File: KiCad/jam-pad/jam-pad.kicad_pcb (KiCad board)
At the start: 2 copper layers, 173 x 57.1 mm, 56 parts, among them J1 USB_C, J2 PH_01x03_2.54mm, SW1 MX_Hotswap, SW13 SW_Push, SW14 RotaryEncoder_Switch, SW15 SW_Push, SW2 MX_Hotswap, SW3 MX_Hotswap, SW4 MX_Hotswap, SW5 MX_Hotswap, SW6 MX_Hotswap, SW7 MX_Hotswap, SW8 MX_Hotswap, SW9 MX_Hotswap, U1 RP2040, U2 OLED_RGB_128x128_waveshare, U3 W25Q16JVSNIQ, U4 MIC5319-3.3YD5, Y1 ECS-120-18-33-JGN

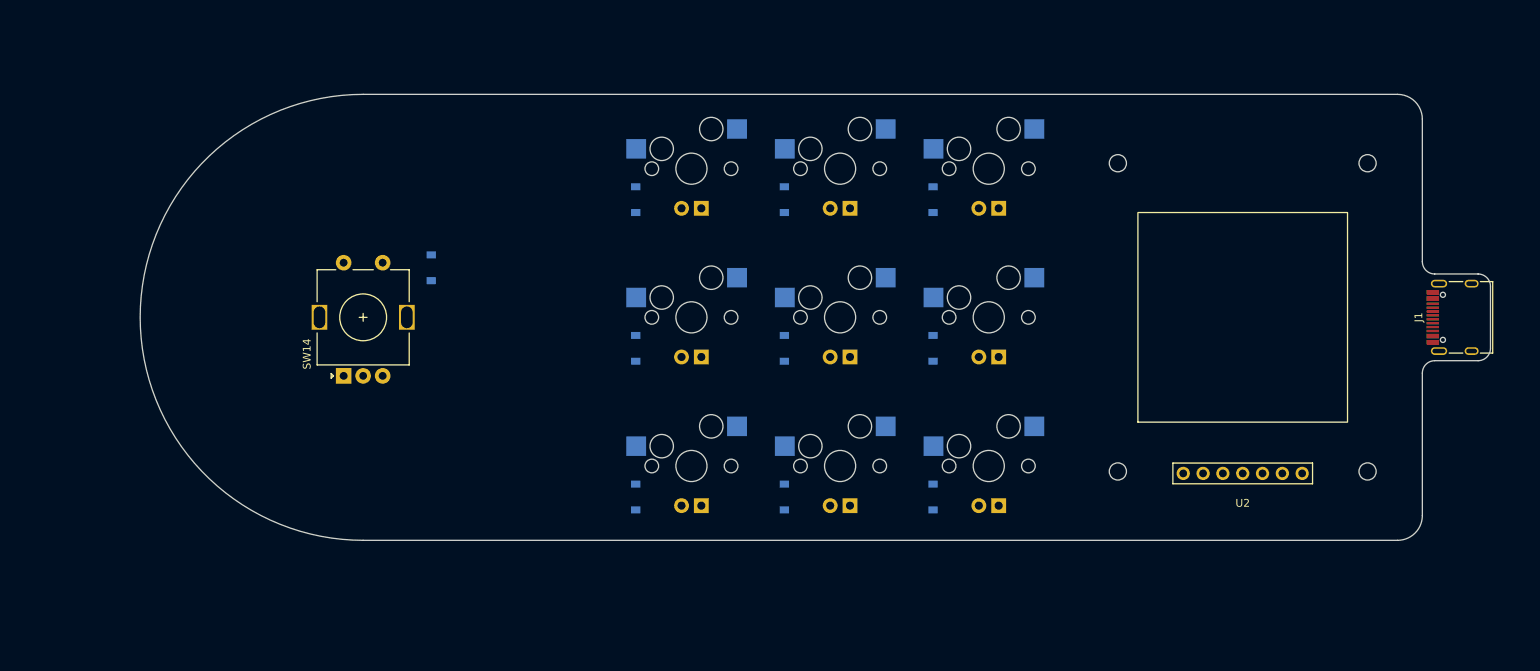
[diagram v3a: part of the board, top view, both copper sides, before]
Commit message: added multi part sym for switch+led, remove backups
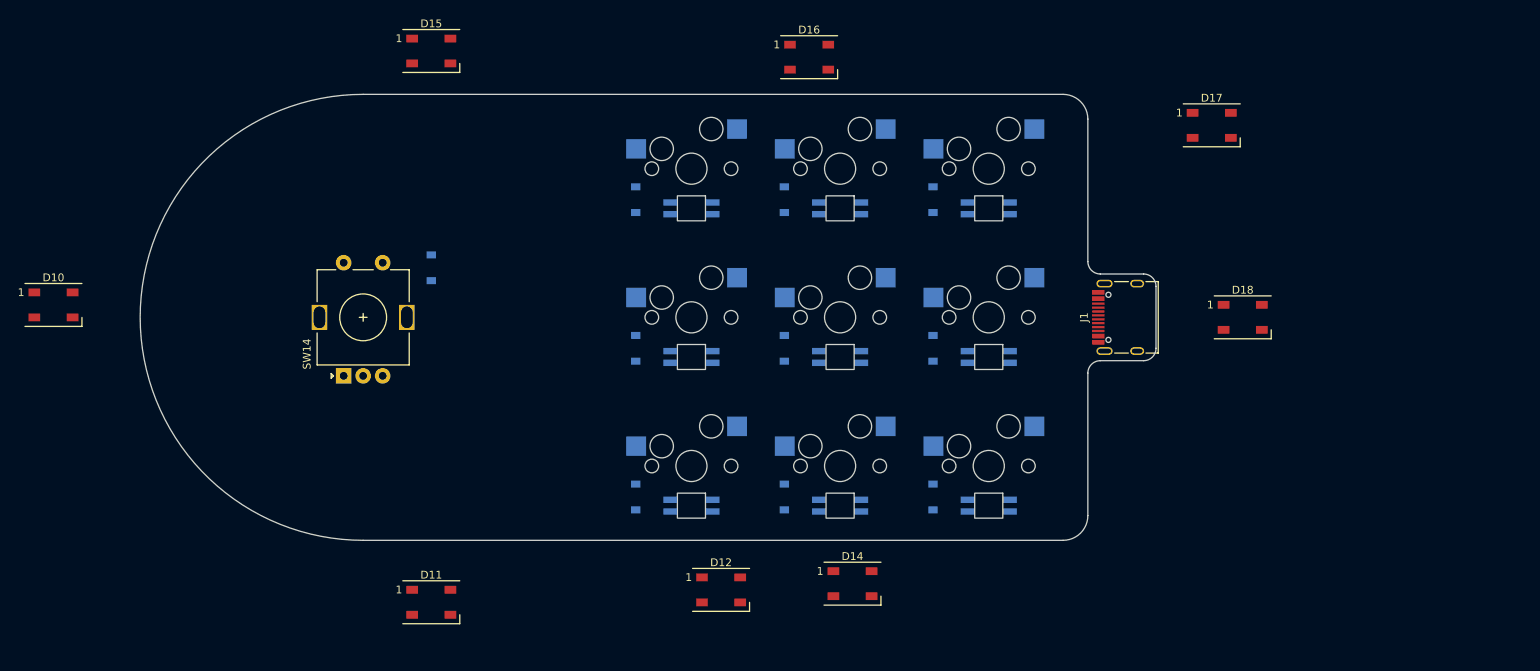
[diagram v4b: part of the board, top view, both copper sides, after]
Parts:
- removed U2: OLED_RGB_128x128_waveshare, jam-pad:Display_Waveshare_OLED_1.5inch_128x128
- added D10: WS2812B, LED_SMD:LED_WS2812B_PLCC4_5.0x5.0mm_P3.2mm, F.Cu at (20.6, 52.4)
- added D11: WS2812B, LED_SMD:LED_WS2812B_PLCC4_5.0x5.0mm_P3.2mm, F.Cu at (69.1, 90.5)
- added D12: WS2812B, LED_SMD:LED_WS2812B_PLCC4_5.0x5.0mm_P3.2mm, F.Cu at (106.2, 88.9)
- added D14: WS2812B, LED_SMD:LED_WS2812B_PLCC4_5.0x5.0mm_P3.2mm, F.Cu at (123.0, 88.1)
- added D15: WS2812B, LED_SMD:LED_WS2812B_PLCC4_5.0x5.0mm_P3.2mm, F.Cu at (69.1, 19.8)
- added D16: WS2812B, LED_SMD:LED_WS2812B_PLCC4_5.0x5.0mm_P3.2mm, F.Cu at (117.5, 20.6)
- added D17: WS2812B, LED_SMD:LED_WS2812B_PLCC4_5.0x5.0mm_P3.2mm, F.Cu at (169.1, 29.4)
- added D18: WS2812B, LED_SMD:LED_WS2812B_PLCC4_5.0x5.0mm_P3.2mm, F.Cu at (173.0, 54.0)
- SW1, SW2, SW3, SW4, SW5, SW6, SW7, SW8, SW9: value MX_Hotswap -> MX_Hotswap_LED_RGB; footprint MX_Only:MXOnly-1U-Hotswap-LED -> jam-pad:MXOnly-1U-Hotswap-SK6812MINI-E
- moved J1 42.9 mm to (155.3, 54.0)
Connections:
- SW1 pad 3: (no net) -> +3V3
- SW1 pad 4: (no net) -> /Backlight
- SW2 pad 3: (no net) -> +3V3
- SW2 pad 4: (no net) -> Net-(SW1-Pad5)
- SW3 pad 3: (no net) -> +3V3
- SW3 pad 4: (no net) -> Net-(SW2-Pad5)
- SW4 pad 3: (no net) -> +3V3
- SW4 pad 4: (no net) -> Net-(SW4-Pad4)
- SW5 pad 3: (no net) -> +3V3
- SW5 pad 4: (no net) -> Net-(SW5-Pad4)
- SW6 pad 3: (no net) -> +3V3
- SW6 pad 4: (no net) -> Net-(SW3-Pad5)
- SW7 pad 3: (no net) -> +3V3
- SW7 pad 4: (no net) -> Net-(SW4-Pad5)
- SW8 pad 3: (no net) -> +3V3
- SW8 pad 4: (no net) -> Net-(SW7-Pad5)
- SW9 pad 3: (no net) -> +3V3
- SW9 pad 4: (no net) -> Net-(SW8-Pad5)
- U1 pad 11: /SCLK -> /Backlight
- U1 pad 12: /CS -> unconnected-(U1-Pad12)
- U1 pad 13: /DC -> unconnected-(U1-Pad13)
- U1 pad 14: /OLED_RST -> unconnected-(U1-Pad14)
- U1 pad 9: /MOSI -> unconnected-(U1-Pad9)
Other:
- board size 173 x 57.1 mm -> 130.2 x 57.1 mm

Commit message: Add JLCPCB design rules and preliminary route MCU
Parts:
- moved C11 0.14 mm to (70.4, 134.4)
- moved C12 0.14 mm to (69.9, 151.4)
- moved C13 0.14 mm to (65.4, 134.4)
- moved C14 0.14 mm to (76.4, 136.9)
- moved C16 0.14 mm to (69.9, 155.9)
- moved C3 0.14 mm to (72.9, 134.4)
- moved C5 0.14 mm to (67.4, 134.4)
- moved C6 0.14 mm to (76.4, 139.4)
- moved C7 0.14 mm to (76.4, 143.9)
- moved C8 0.14 mm to (67.4, 151.4)
- moved J2 0.14 mm to (74.4, 160.9)
- moved R10 0.14 mm to (73.9, 151.4)
- moved R4 0.14 mm to (76.4, 134.4)
- moved R6 0.14 mm to (67.9, 129.4)
- moved R7 0.14 mm to (70.2, 129.4)
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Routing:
- net +3V3: track 0.00 -> 39.0 mm, vias 0 -> 2
- net +1V1: track 0.00 -> 14.5 mm
- net /VREF_ADC: track 0.00 -> 9.97 mm
- net Net-(C16-Pad2): track 0.00 -> 7.78 mm
- net /~{RESET}: track 0.00 -> 7.46 mm
- net Net-(R8-Pad2): track 0.00 -> 4.93 mm

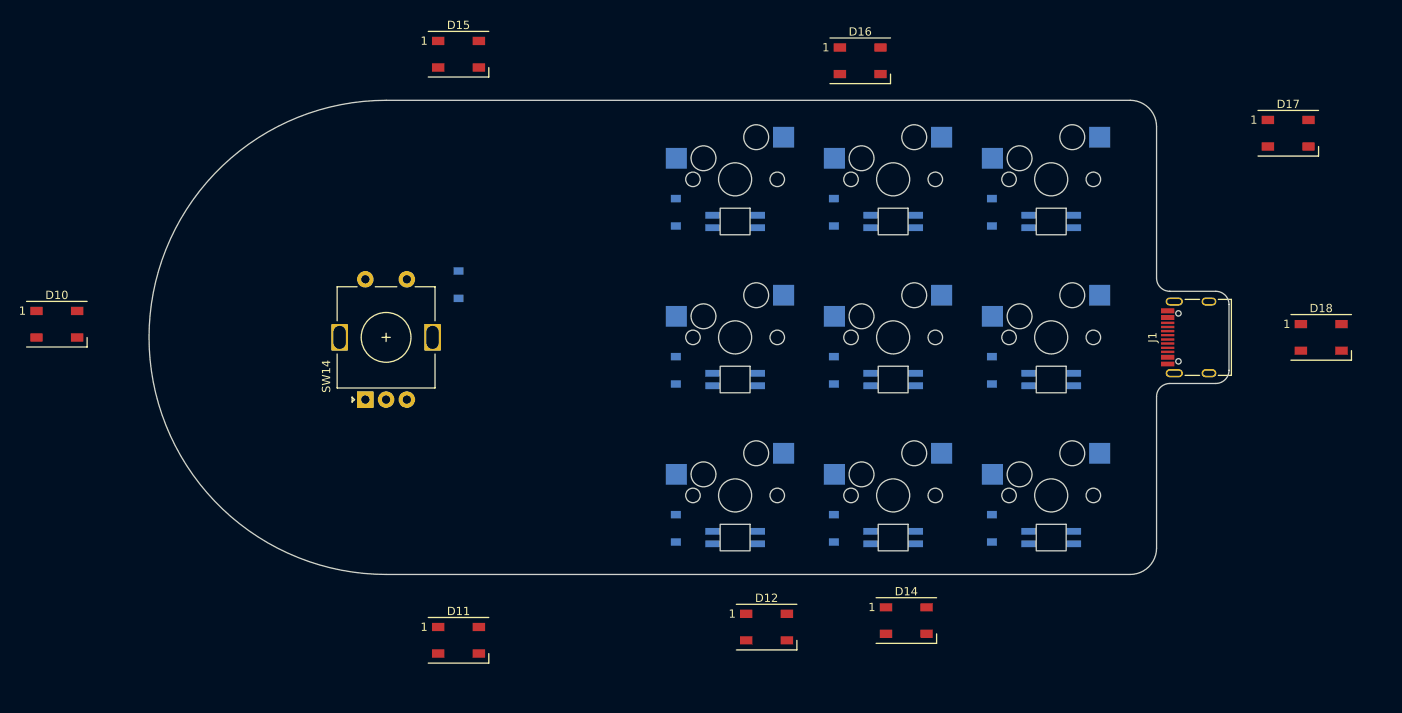
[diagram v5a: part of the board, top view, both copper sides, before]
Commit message: changed underglow to knoblight, added led c and r, placed leds
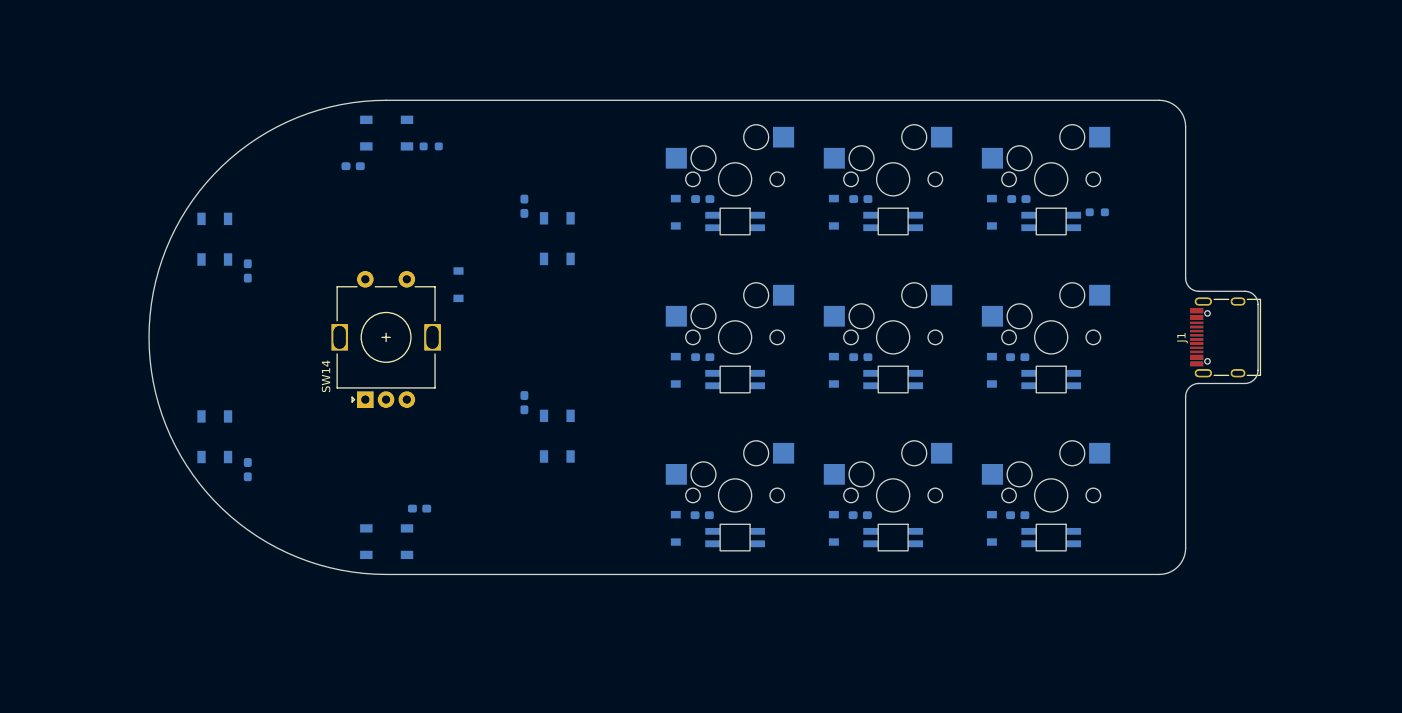
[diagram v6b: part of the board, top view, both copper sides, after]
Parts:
- removed D14, D18: WS2812B, LED_SMD:LED_WS2812B_PLCC4_5.0x5.0mm_P3.2mm
- added C17: .1u, Capacitor_SMD:C_0603_1608Metric_Pad1.08x0.95mm_HandSolder, B.Cu at (98.5, 37.3)
- added C18: .1u, Capacitor_SMD:C_0603_1608Metric_Pad1.08x0.95mm_HandSolder, B.Cu at (117.5, 37.3)
- added C19: .1u, Capacitor_SMD:C_0603_1608Metric_Pad1.08x0.95mm_HandSolder, B.Cu at (136.6, 37.3)
- added C20: .1u, Capacitor_SMD:C_0603_1608Metric_Pad1.08x0.95mm_HandSolder, B.Cu at (136.5, 56.4)
- added C21: .1u, Capacitor_SMD:C_0603_1608Metric_Pad1.08x0.95mm_HandSolder, B.Cu at (117.5, 56.4)
- added C22: .1u, Capacitor_SMD:C_0603_1608Metric_Pad1.08x0.95mm_HandSolder, B.Cu at (98.5, 56.4)
- added C23: .1u, Capacitor_SMD:C_0603_1608Metric_Pad1.08x0.95mm_HandSolder, B.Cu at (98.4, 75.4)
- added C24: .1u, Capacitor_SMD:C_0603_1608Metric_Pad1.08x0.95mm_HandSolder, B.Cu at (117.5, 75.4)
- added C25: .1u, Capacitor_SMD:C_0603_1608Metric_Pad1.08x0.95mm_HandSolder, B.Cu at (136.5, 75.4)
- added C26: .1u, Capacitor_SMD:C_0603_1608Metric_Pad1.08x0.95mm_HandSolder, B.Cu at (56.4, 33.3)
- added C27: .1u, Capacitor_SMD:C_0603_1608Metric_Pad1.08x0.95mm_HandSolder, B.Cu at (43.7, 46.0)
- added C28: .1u, Capacitor_SMD:C_0603_1608Metric_Pad1.08x0.95mm_HandSolder, B.Cu at (43.7, 69.9)
- added C30: .1u, Capacitor_SMD:C_0603_1608Metric_Pad1.08x0.95mm_HandSolder, B.Cu at (77.0, 38.2)
- added C31: .1u, Capacitor_SMD:C_0603_1608Metric_Pad1.08x0.95mm_HandSolder, B.Cu at (77.0, 61.8)
- added C32: .1u, Capacitor_SMD:C_0603_1608Metric_Pad1.08x0.95mm_HandSolder, B.Cu at (64.4, 74.6)
- added R11: 300, Resistor_SMD:R_0603_1608Metric_Pad0.98x0.95mm_HandSolder, B.Cu at (146.1, 38.9)
- added R12: 300, Resistor_SMD:R_0603_1608Metric_Pad0.98x0.95mm_HandSolder, B.Cu at (65.8, 31.0)
- D10, D11, D12, D15, D16, D17: moved to B.Cu
- moved D17 119.3 mm to (60.4, 78.6), turned to 180 degrees
- moved D12 70.4 mm to (39.7, 66.0), turned to 90 degrees
- moved D16 58.1 mm to (81.0, 65.9), turned to -90 degrees
- moved D11 56.6 mm to (39.7, 42.1), turned to 90 degrees
- moved D10 45.9 mm to (60.4, 29.4)
- moved D15 25.2 mm to (81.0, 42.1), turned to -90 degrees
- moved J1 3.50 mm to (158.8, 54.0)
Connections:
- D10 pad 4: /Underglow -> Net-(D10-DIN)
- D12 pad 2: Net-(D12-Pad2) -> Net-(D12-DOUT)
- D17 pad 4: Net-(D17-Pad4) -> Net-(D12-DOUT)
- SW1 pad 4: /Backlight -> Net-(SW1B-DIN)
- SW1 pad 5: Net-(SW1-Pad5) -> Net-(SW1B-DOUT)
- SW2 pad 4: Net-(SW1-Pad5) -> Net-(SW2B-DIN)
- SW2 pad 5: Net-(SW2-Pad5) -> Net-(SW1B-DIN)
- SW3 pad 4: Net-(SW2-Pad5) -> Net-(SW3B-DIN)
- SW3 pad 5: Net-(SW3-Pad5) -> Net-(SW2B-DIN)
- SW4 pad 5: Net-(SW4-Pad5) -> Net-(SW4B-DOUT)
- SW6 pad 4: Net-(SW3-Pad5) -> Net-(SW1B-DOUT)
- SW7 pad 4: Net-(SW4-Pad5) -> Net-(SW7B-DIN)
- SW7 pad 5: Net-(SW7-Pad5) -> unconnected-(SW7B-DOUT-Pad5)
- SW8 pad 4: Net-(SW7-Pad5) -> Net-(SW8B-DIN)
- SW8 pad 5: Net-(SW8-Pad5) -> Net-(SW7B-DIN)
- SW9 pad 4: Net-(SW8-Pad5) -> Net-(SW4B-DOUT)
- SW9 pad 5: unconnected-(SW9-Pad5) -> Net-(SW8B-DIN)
- U1 pad 12: unconnected-(U1-Pad12) -> /Knob_Light
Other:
- board size 130.2 x 57.1 mm -> 133.7 x 57.1 mm

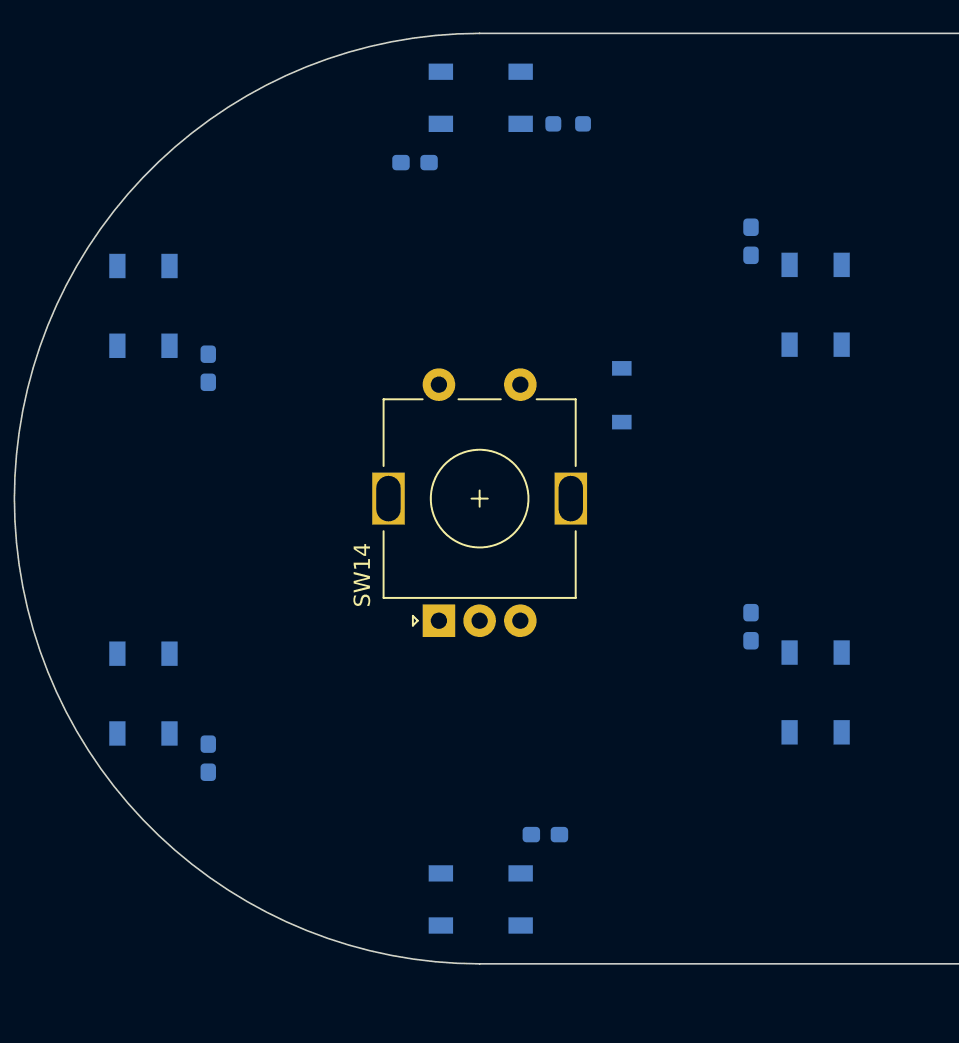
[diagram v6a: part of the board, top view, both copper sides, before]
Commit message: knob leds moved to top
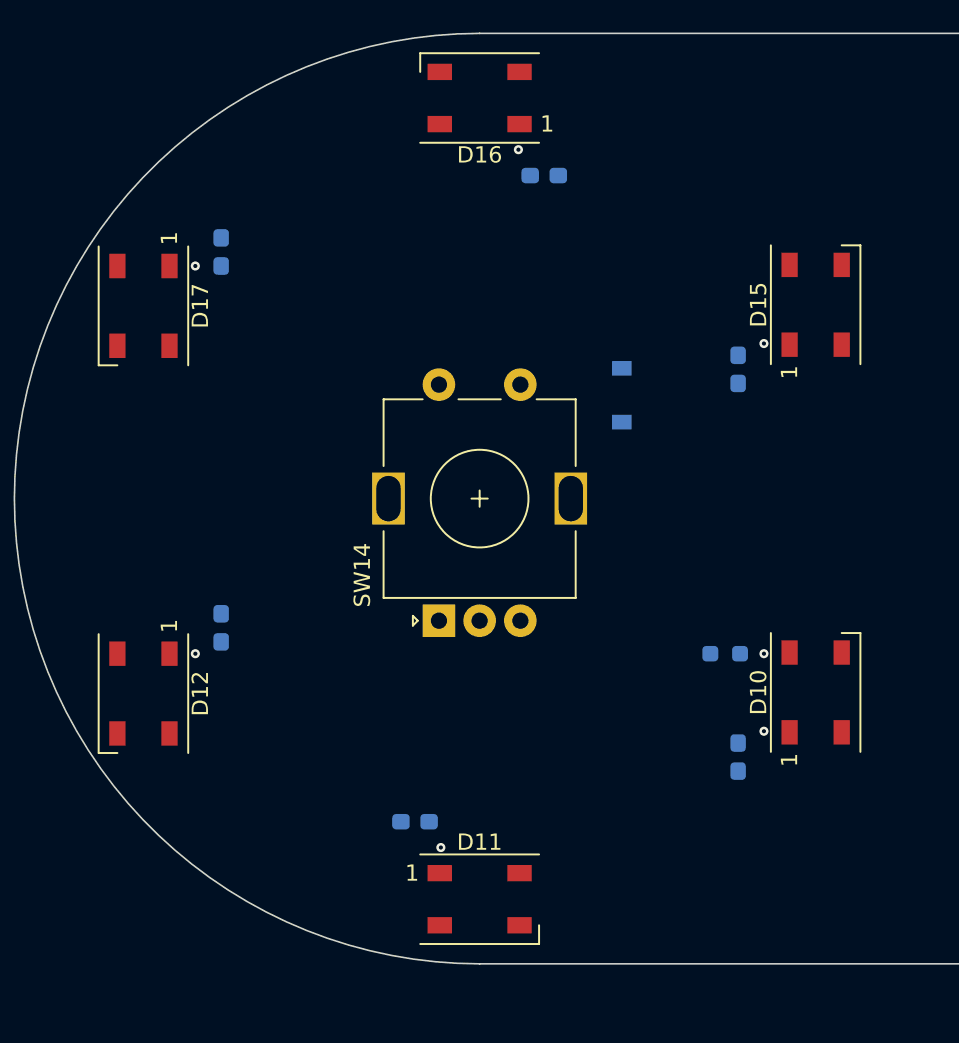
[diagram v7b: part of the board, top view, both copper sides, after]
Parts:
- D10, D11, D12, D15, D16, D17: moved to F.Cu
- moved D16 41.9 mm to (60.3, 29.4), turned to 180 degrees
- moved D17 41.9 mm to (39.7, 42.1), turned to -90 degrees
- moved D10 41.9 mm to (81.0, 65.9), turned to 90 degrees
- moved D11 41.9 mm to (60.3, 78.6), turned to 0 degrees
- moved C26 41.6 mm to (76.2, 69.8), turned to 90 degrees
- moved C32 41.0 mm to (44.5, 38.8), turned to -90 degrees
- moved R12 33.9 mm to (75.4, 63.5), turned to 0 degrees
- moved C27 30.6 mm to (56.4, 73.8), turned to 0 degrees
- moved C31 30.5 mm to (64.3, 34.1), turned to 180 degrees
- moved C28 8.05 mm to (44.5, 61.9), turned to -90 degrees
- moved C30 7.91 mm to (76.2, 46.0), turned to 90 degrees
- turned D12 to -90 degrees
- turned D15 to 90 degrees
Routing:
- net (no net): vias 0 -> 7

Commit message: initial routing
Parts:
- SW1, SW2, SW3, SW7, SW8, SW9: footprint jam-pad:MXOnly-1U-Hotswap-SK6812MINI-E -> jam-pad:MXOnly-1U-Hotswap-SK6812MINI-E_180
- moved R11 46.2 mm to (100.0, 42.9), turned to 0 degrees
- moved C25 8.49 mm to (142.9, 81.0)
- moved C23 8.44 mm to (104.8, 81.0)
- moved C24 8.44 mm to (123.8, 81.0)
- moved C17 8.39 mm to (104.8, 42.9)
- moved C18 8.39 mm to (123.8, 42.9)
- moved C19 8.39 mm to (142.9, 42.9)
- moved C28 0.73 mm to (44.5, 62.6)
- moved C30 0.73 mm to (76.2, 45.3)
- moved C31 0.73 mm to (63.6, 34.1)
- moved C26 0.72 mm to (76.2, 69.1)
- moved C27 0.72 mm to (57.1, 73.8)
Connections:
- R11 pad 2: Net-(SW3B-DIN) -> Net-(SW1B-DIN)
- SW2 pad 4: Net-(SW2B-DIN) -> Net-(SW1B-DOUT)
- SW2 pad 5: Net-(SW1B-DIN) -> Net-(SW2B-DOUT)
- SW3 pad 4: Net-(SW3B-DIN) -> Net-(SW2B-DOUT)
- SW3 pad 5: Net-(SW2B-DIN) -> Net-(SW3B-DOUT)
- SW6 pad 4: Net-(SW1B-DOUT) -> Net-(SW3B-DOUT)
- SW7 pad 4: Net-(SW7B-DIN) -> Net-(SW4B-DOUT)
- SW7 pad 5: unconnected-(SW7B-DOUT-Pad5) -> Net-(SW7B-DOUT)
- SW8 pad 4: Net-(SW8B-DIN) -> Net-(SW7B-DOUT)
- SW8 pad 5: Net-(SW7B-DIN) -> Net-(SW8B-DOUT)
- SW9 pad 4: Net-(SW4B-DOUT) -> Net-(SW8B-DOUT)
- SW9 pad 5: Net-(SW8B-DIN) -> unconnected-(SW9B-DOUT-Pad5)
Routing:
- net Row0: track 0.00 -> 42.8 mm
- net Row2: track 0.00 -> 42.8 mm
- net Row1: track 0.00 -> 42.8 mm, vias 0 -> 4
- net Col1: track 0.00 -> 40.3 mm, vias 0 -> 4
- net Col0: track 0.00 -> 40.3 mm, vias 0 -> 4
- net Col2: track 0.00 -> 40.3 mm
- net +3V3: track 39.0 -> 78.5 mm, vias 2 -> 8
- net Net-(SW4B-DOUT): track 0.00 -> 31.7 mm
- net Net-(SW3B-DOUT): track 0.00 -> 25.4 mm
- net Net-(SW8B-DOUT): track 0.00 -> 15.4 mm
- net Net-(SW5B-DIN): track 0.00 -> 15.4 mm
- net Net-(SW2B-DOUT): track 0.00 -> 15.4 mm
- net Net-(SW1B-DOUT): track 0.00 -> 15.4 mm
- net Net-(SW7B-DOUT): track 0.00 -> 15.4 mm
- net Net-(SW4B-DIN): track 0.00 -> 15.4 mm
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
